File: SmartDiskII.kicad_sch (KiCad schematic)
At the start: 45 parts, among them J1 Apple II Expansion Slot, J2 DRV, U1 74LS174, U10 27C256, U11 74LS245, U12 74LS323, U13 74LS00, U14 74LS174, U2 NE556, U3 74LS05, U4 74LS132, U5 74LS259/9334, U6 74LS20, U7 74LS21, U8 2758/16/32 P6, U9 74LS30

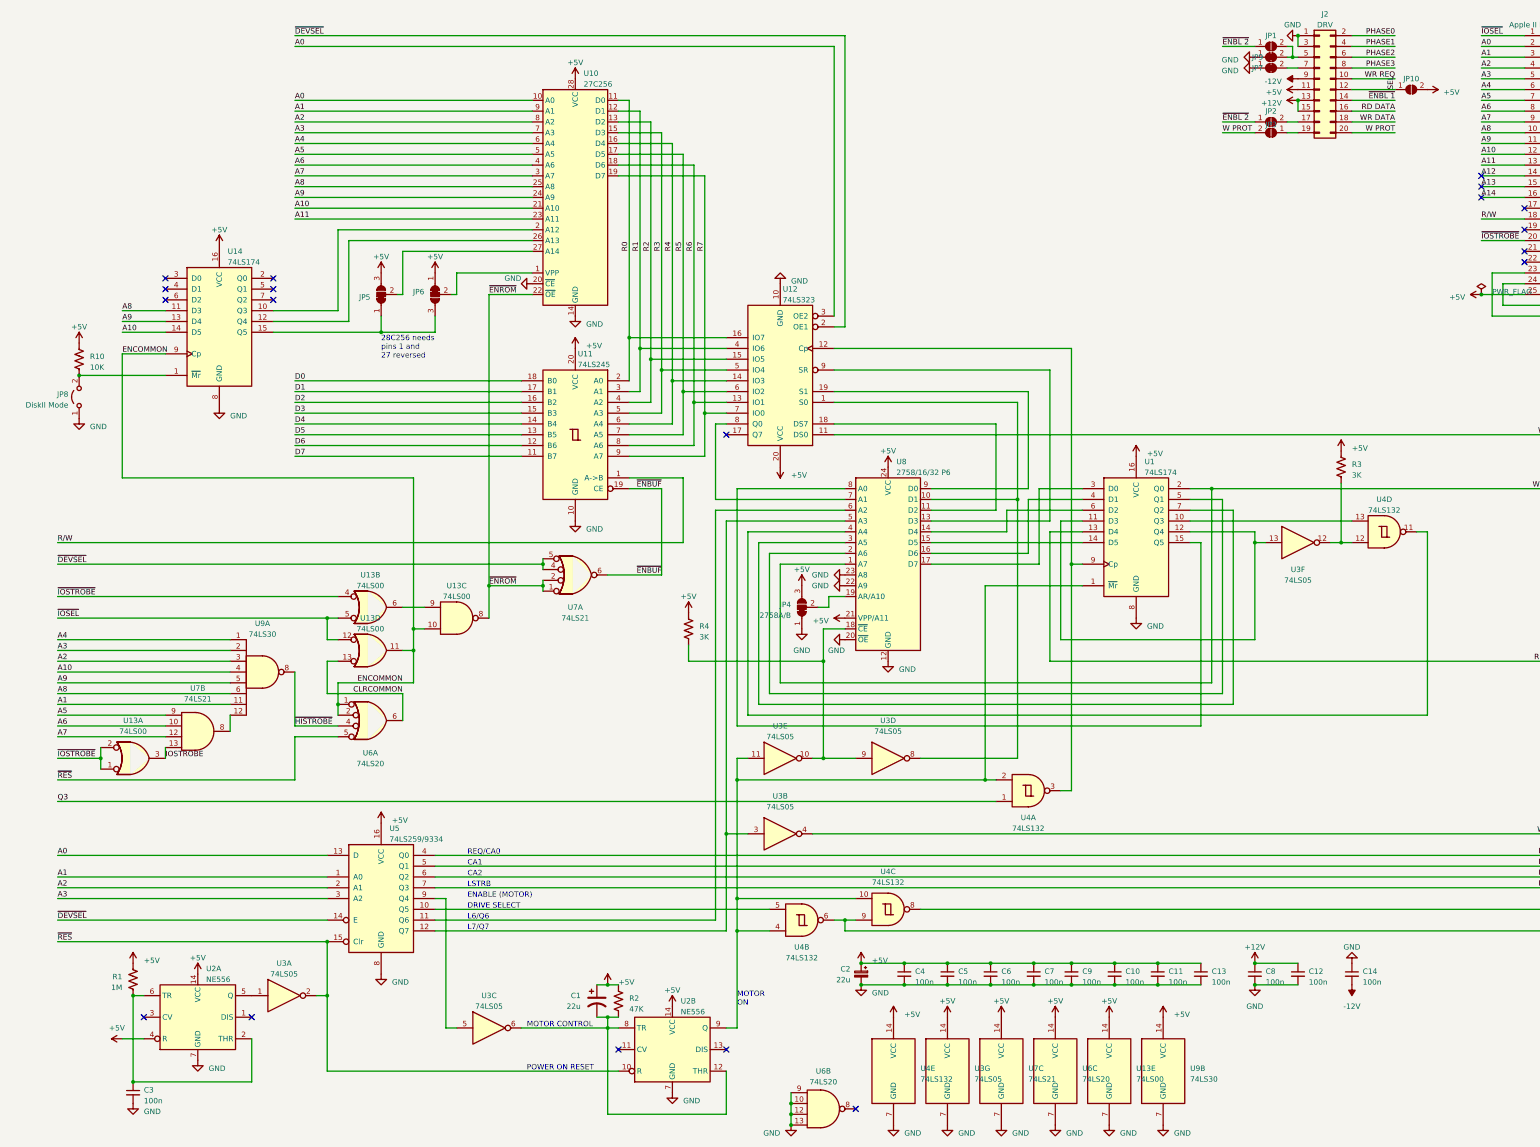
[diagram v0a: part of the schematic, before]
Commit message: invert /SEL for auto detect of 5.25 floppy
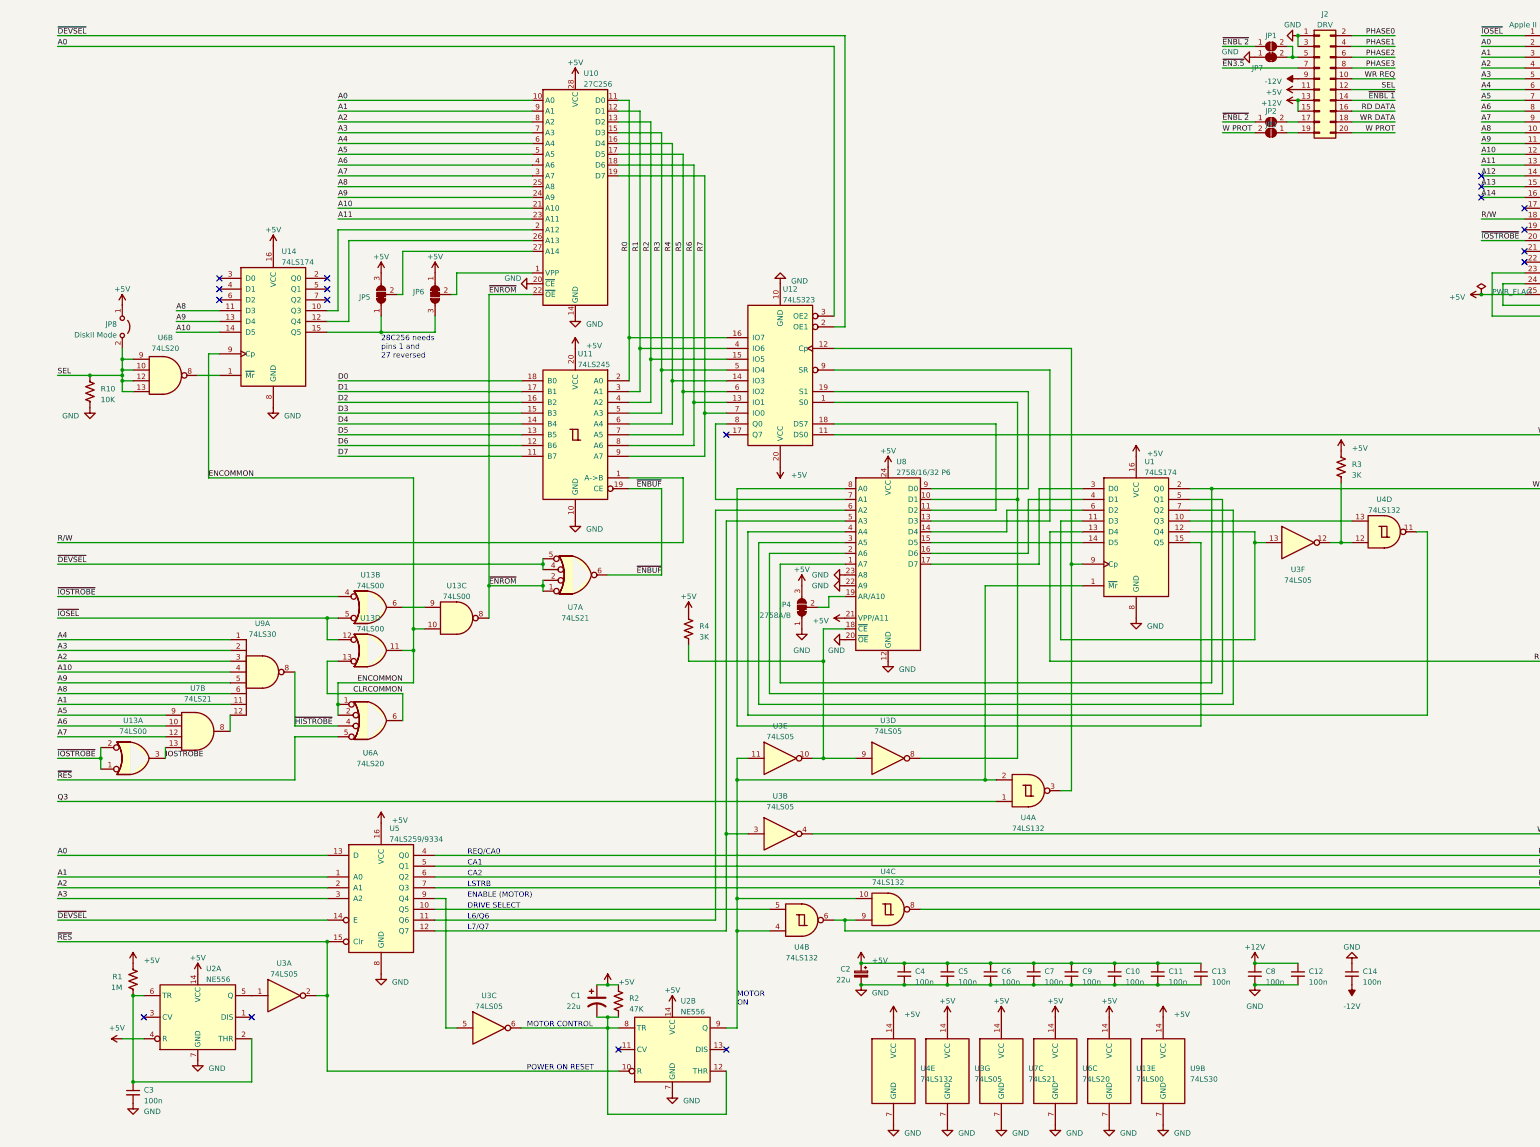
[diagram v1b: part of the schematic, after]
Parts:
- removed JP10: ~, Jumper:SolderJumper-2_P1.3mm_Open_RoundedPad1.0x1.5mm, symbol Jumper:SolderJumper_2_Open
- removed JP9: ~, Jumper:SolderJumper-2_P1.3mm_Bridged_RoundedPad1.0x1.5mm, symbol Jumper:SolderJumper_2_Bridged
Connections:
- net +5V: now also JP8.1 (A); no longer R10.2
- net GND: now also R10.2; no longer JP8.1 (A), U6.10, U6.12, U6.13, U6.9
- net SEL: now also JP8.2 (B), R10.1, U6.10, U6.12, U6.13, U6.9
- net at U6.8: now also U14.1 (~{Mr})
- net ~{EN3.5}: now reaches J2.7 (Pin_7)
- no-connect marks 28 -> 27
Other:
- moved on the sheet: JP8, R10, U14, U6B

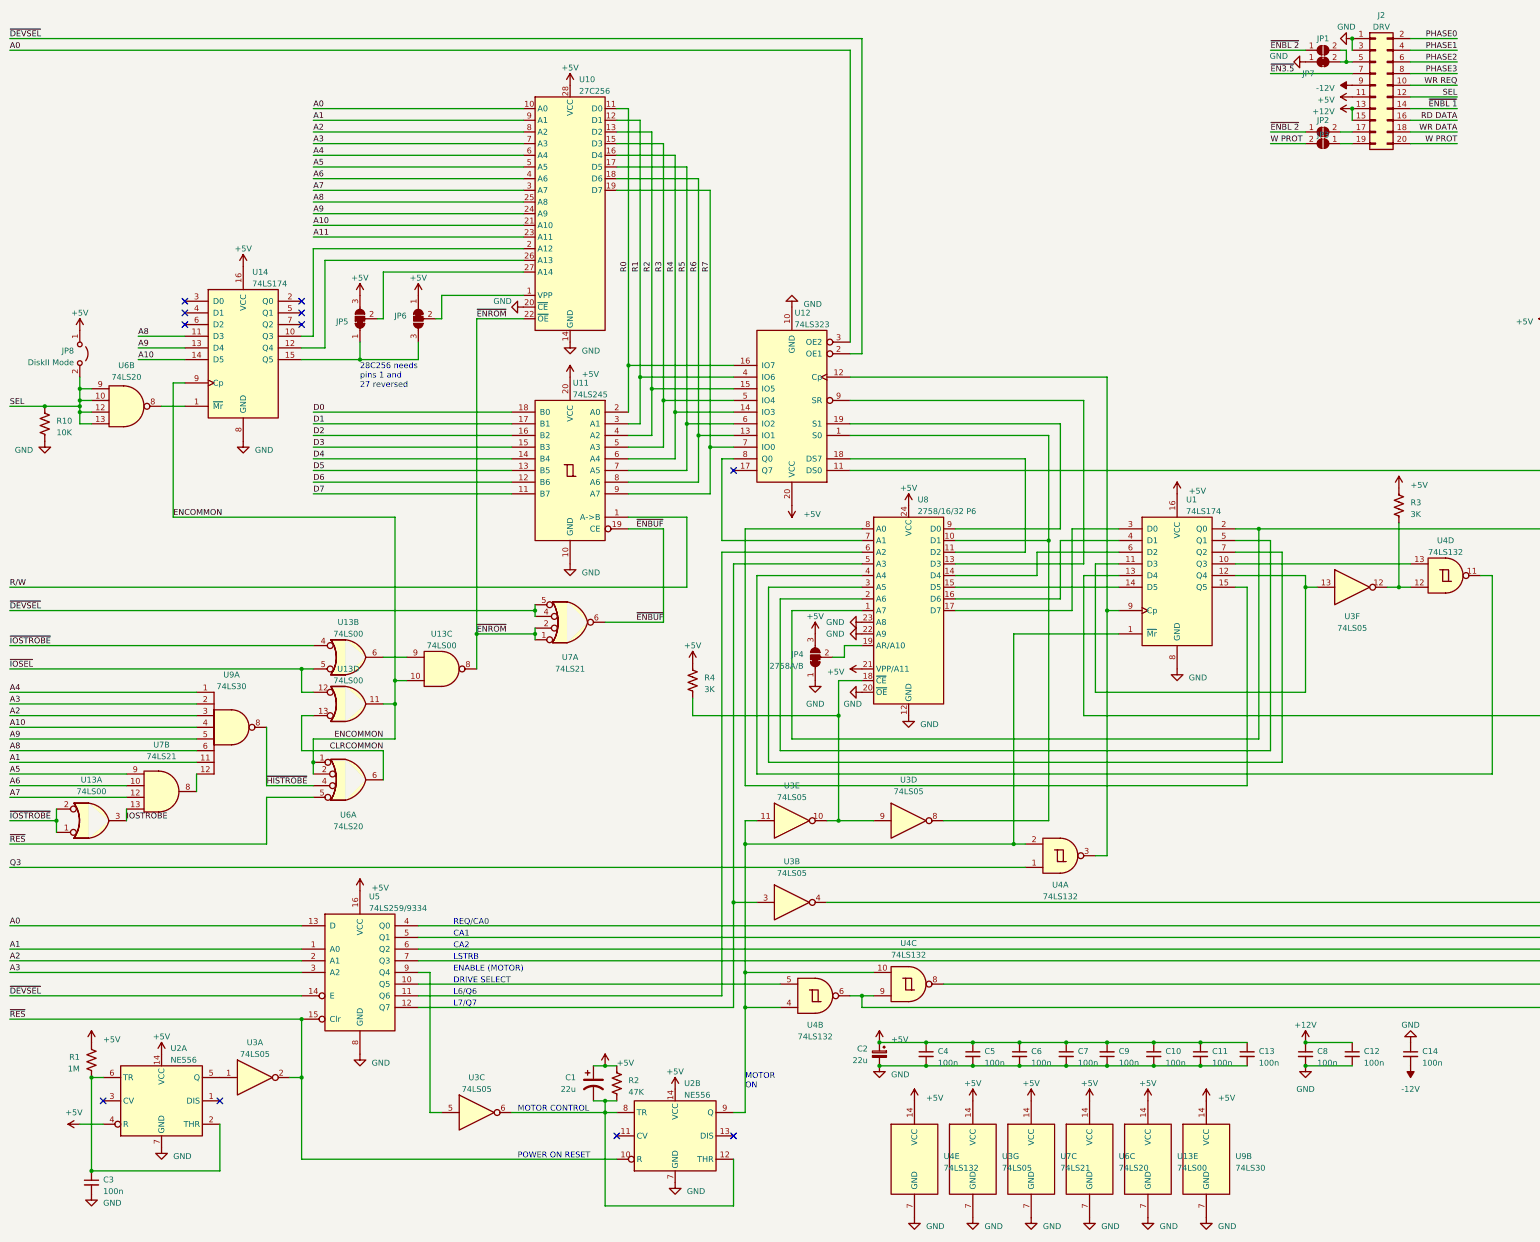
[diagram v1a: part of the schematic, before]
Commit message: readd second floppy connector
reference number changes
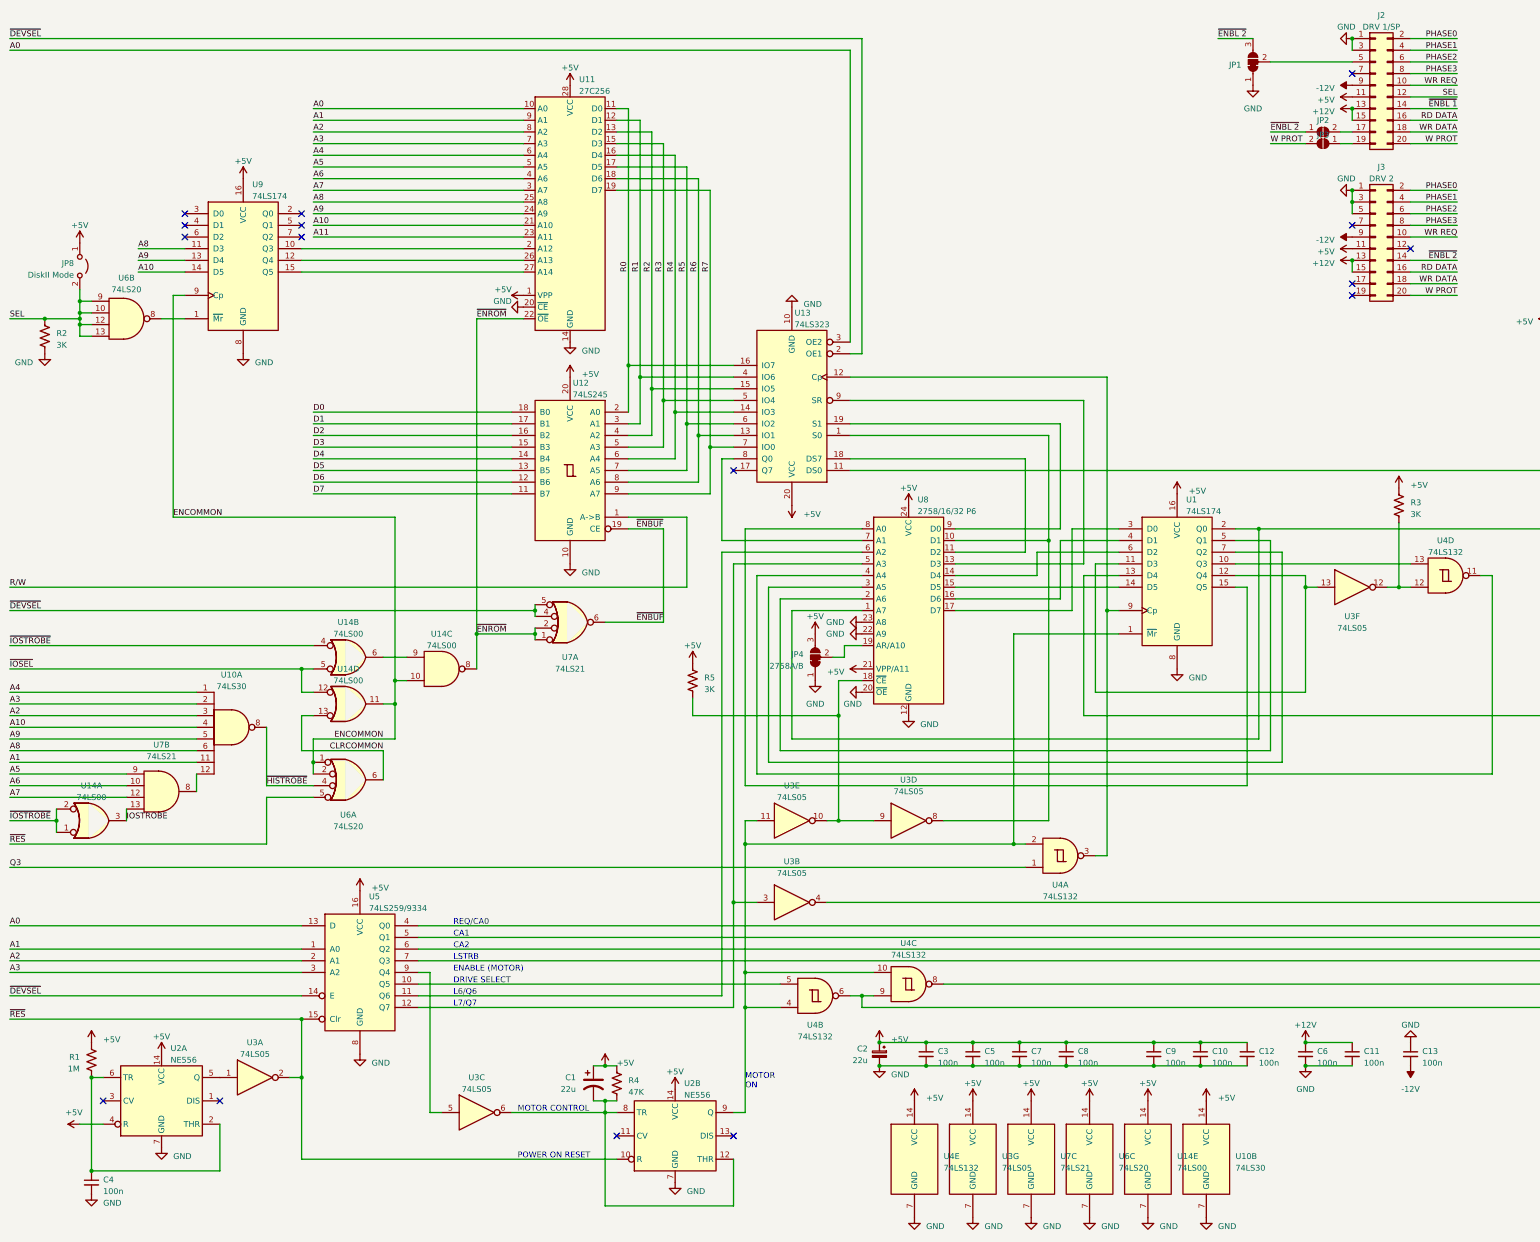
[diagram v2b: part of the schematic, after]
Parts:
- removed C9: 100n, Capacitor_THT:C_Disc_D4.3mm_W1.9mm_P5.00mm, symbol Device:C_Small
- removed JP1: ~, Jumper:SolderJumper-2_P1.3mm_Open_RoundedPad1.0x1.5mm, symbol Jumper:SolderJumper_2_Open
- removed JP5, JP6: ~, Jumper:SolderJumper-3_P1.3mm_Bridged12_RoundedPad1.0x1.5mm_NumberLabels, symbol Jumper:SolderJumper_3_Bridged12
- removed JP7: ~, Jumper:SolderJumper-2_P1.3mm_Bridged_RoundedPad1.0x1.5mm, symbol Jumper:SolderJumper_2_Bridged
- added J3: DRV 2, MyConnector:PinHeader_2x10_P2.54mm_Vertical_Shrouded, symbol Connector_Generic:Conn_02x10_Odd_Even
- added JP1: ~, Jumper:SolderJumper-3_P1.3mm_Bridged12_RoundedPad1.0x1.5mm_NumberLabels, symbol Jumper:SolderJumper_3_Bridged12
- J2: value DRV -> DRV 1/SP
- R2: renamed from R10; value 10K -> 3K
- renumbered C11 to C10, C12 to C11, C13 to C12, C14 to C13, C4 to C3, C3 to C4, C8 to C6, C6 to C7, C7 to C8, C10 to C9, R2 to R4, R4 to R5, U9 to U10, U10 to U11, U11 to U12, U12 to U13, U13 to U14, U14 to U9
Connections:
- net +12V: now also J3.13 (Pin_13), J3.15 (Pin_15)
- net +5V: now also U11.1 (VPP), J3.11 (Pin_11)
- net -12V: now also J3.9 (Pin_9)
- net GND: now also J3.1 (Pin_1), J3.3 (Pin_3), J3.5 (Pin_5), JP1.1 (A)
- net PHASE0: now also J3.2 (Pin_2)
- net PHASE1: now also J3.4 (Pin_4)
- net PHASE2: now also J3.6 (Pin_6)
- net PHASE3: now also J3.8 (Pin_8)
- net RD DATA: now also J3.16 (Pin_16)
- net W PROT: now also J3.20 (Pin_20)
- net WR DATA: now also J3.18 (Pin_18)
- net WR REQ: now also J3.10 (Pin_10)
- net ~{ENBL 2}: now also J3.14 (Pin_14), JP1.3 (B)
- net at U9.15 (Q5): now also U11.27 (A14)
- net at J2.5 (Pin_5): now also JP1.2 (C)
- net ~{EN3.5}: no longer names the net of J2.7 (Pin_7)
- no-connect marks 27 -> 32
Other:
- note removed: "28C256 needs pins 1 and 27 reversed"
- moved on the sheet: JP8, R2, U6B, U9
